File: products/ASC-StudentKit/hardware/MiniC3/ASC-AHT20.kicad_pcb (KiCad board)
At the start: 2 copper layers, 48 x 6 mm, 3 parts, among them J1 CABLE, U1 AHT20

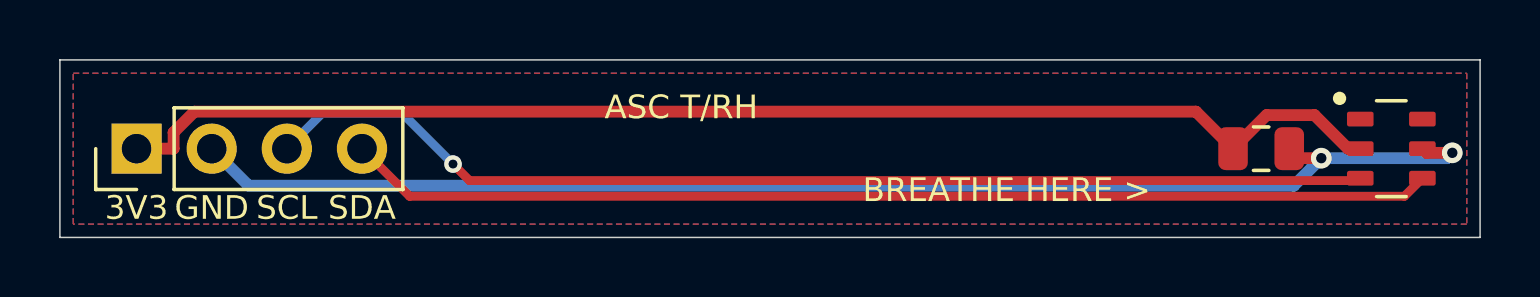
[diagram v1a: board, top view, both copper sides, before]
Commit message: ASC Mini-C3: ULN2003A driver, combo flow connector, assembly markings
- ULN2003A (LCSC C7512) drives the pump (ch 1+2) and the relay (ch 3);
  replaces 2 x AO3400A, 3 x B5819W and 4 resistors, as on FG1
- Flow input: one footprint takes a JST-XH (bench) or a 3.5 mm 3-pole
  screw terminal (FG1 field cable)
- Screw terminals now Phoenix PT-1,5 3.5 mm (KF350 type, library 3D);
  relay output is a pluggable MSTBVA 5.08 header like FG1's
- 1206 LEDs for hand soldering; ref + value labels on every part
  (R3 1K, U3 ULN2003 ...), "1" at IC pin 1, "+" at LED/diode anodes;
  back reads "Agri Sensors and Controls  Oct 2026"
- Re-routed, DRC clean (mains 5 mm), panel and fab regenerated
- Sourcing BOM: 1206 LED and ULN2003A LCSC numbers, CR2032 holder as an
  alternative to the tabbed cell; kit about Rs 967

Co-Authored-By: Claude Opus 5.5 <noreply@anthropic.com>
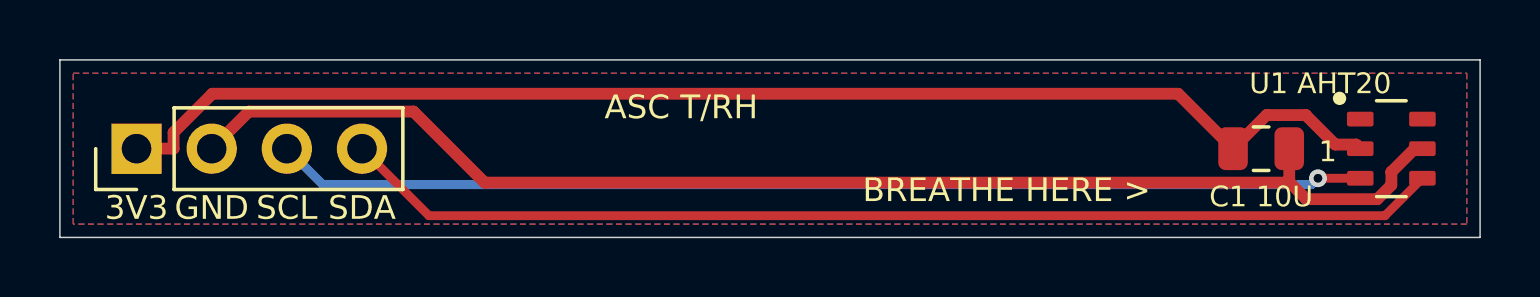
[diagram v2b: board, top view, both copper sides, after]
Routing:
- net /SCL: track 37.8 -> 36.9 mm
- net /SDA: track 36.8 -> 37.3 mm
- net +3V3: track 43.7 -> 44.2 mm
- net GND: track 45.2 -> 44.8 mm, vias 2 -> 0
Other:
- board text added: "1"
- board text added: "C1 10U"
- board text added: "U1 AHT20"
